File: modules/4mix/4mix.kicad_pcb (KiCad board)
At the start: 4 copper layers, 91.4 x 68.6 mm, 6 parts

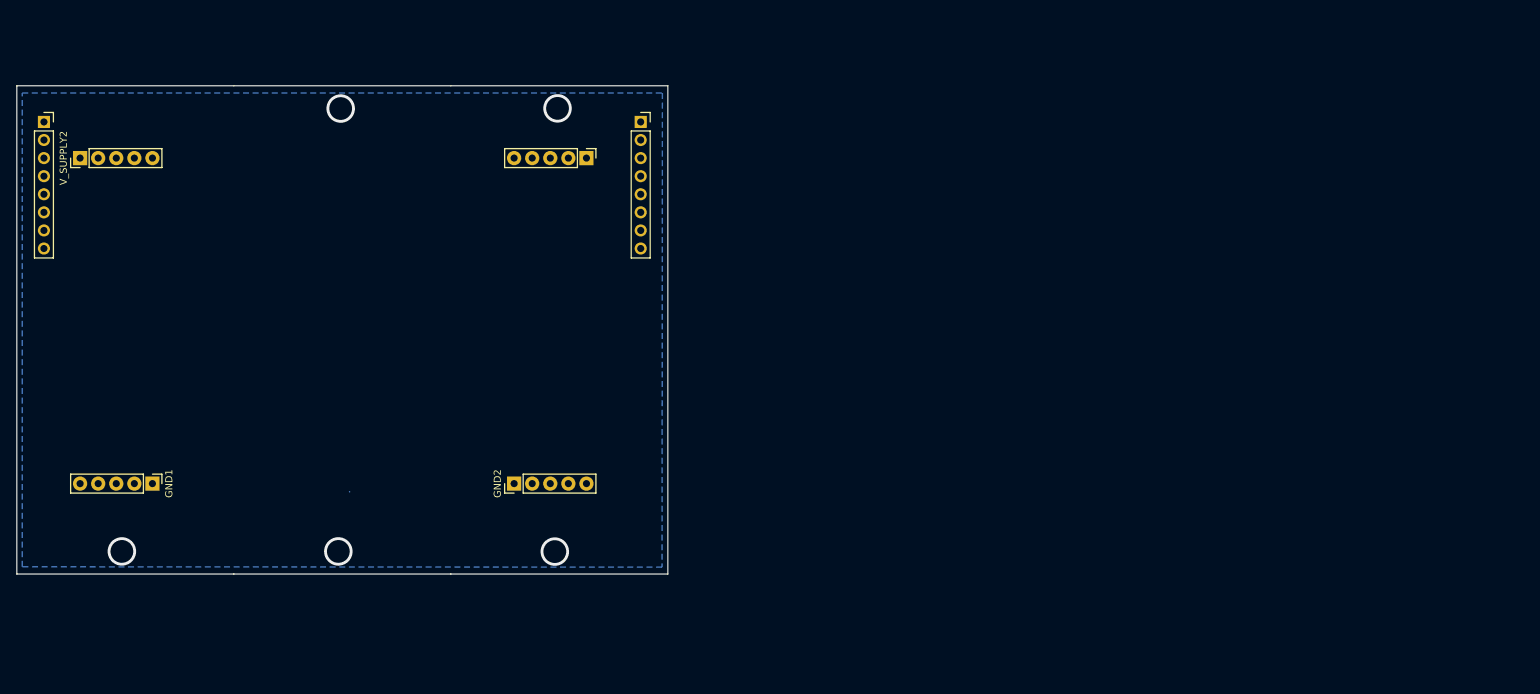
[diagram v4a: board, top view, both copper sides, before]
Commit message: Implement channel 1 routing
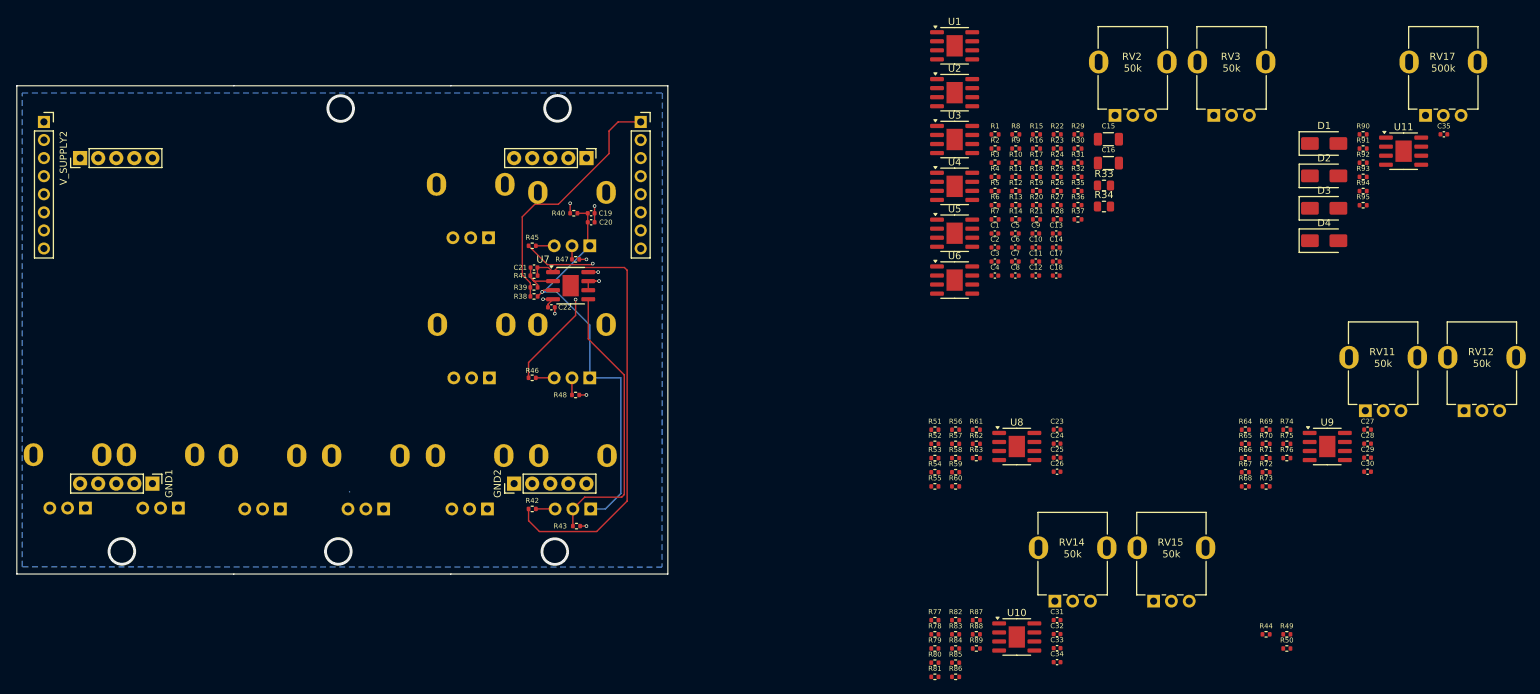
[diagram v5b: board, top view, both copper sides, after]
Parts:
- added C1: 100pf, Capacitor_SMD:C_0402_1005Metric, F.Cu at (184.4, 61.4)
- added C10: 47pf, Capacitor_SMD:C_0402_1005Metric, F.Cu at (190.1, 63.4)
- added C11: 0.1uf, Capacitor_SMD:C_0402_1005Metric, F.Cu at (190.1, 65.3)
- added C12: 0.1uf, Capacitor_SMD:C_0402_1005Metric, F.Cu at (190.1, 67.3)
- added C13: 0.1uf, Capacitor_SMD:C_0402_1005Metric, F.Cu at (193.0, 61.4)
- added C14: 0.1uf, Capacitor_SMD:C_0402_1005Metric, F.Cu at (193.0, 63.4)
- added C15: 0.1uf, Capacitor_SMD:C_1206_3216Metric, F.Cu at (200.3, 48.1)
- added C16: 100uf, Capacitor_SMD:C_1206_3216Metric, F.Cu at (200.3, 51.5)
- added C17: 0.1uf, Capacitor_SMD:C_0402_1005Metric, F.Cu at (193.0, 65.3)
- added C18: 0.1uf, Capacitor_SMD:C_0402_1005Metric, F.Cu at (193.0, 67.3)
- added C19: 10uf, Capacitor_SMD:C_0402_1005Metric, F.Cu at (127.7, 58.5)
- added C2: 100pf, Capacitor_SMD:C_0402_1005Metric, F.Cu at (184.4, 63.4)
- added C20: 0.1uf, Capacitor_SMD:C_0402_1005Metric, F.Cu at (127.7, 59.8)
- added C21: 47pf, Capacitor_SMD:C_0402_1005Metric, F.Cu at (119.6, 66.2)
- added C22: 0.1uf, Capacitor_SMD:C_0402_1005Metric, F.Cu at (122.1, 71.8)
- added C23: 10uf, Capacitor_SMD:C_0402_1005Metric, F.Cu at (193.1, 88.9)
- added C24: 0.1uf, Capacitor_SMD:C_0402_1005Metric, F.Cu at (193.1, 90.9)
- added C25: 47pf, Capacitor_SMD:C_0402_1005Metric, F.Cu at (193.1, 92.9)
- added C26: 0.1uf, Capacitor_SMD:C_0402_1005Metric, F.Cu at (193.1, 94.8)
- added C27: 10uf, Capacitor_SMD:C_0402_1005Metric, F.Cu at (236.7, 88.9)
- added C28: 0.1uf, Capacitor_SMD:C_0402_1005Metric, F.Cu at (236.7, 90.9)
- added C29: 47pf, Capacitor_SMD:C_0402_1005Metric, F.Cu at (236.7, 92.9)
- added C3: 47pf, Capacitor_SMD:C_0402_1005Metric, F.Cu at (184.4, 65.3)
- added C30: 0.1uf, Capacitor_SMD:C_0402_1005Metric, F.Cu at (236.7, 94.8)
- added C31: 10uf, Capacitor_SMD:C_0402_1005Metric, F.Cu at (193.1, 115.7)
- added C32: 0.1uf, Capacitor_SMD:C_0402_1005Metric, F.Cu at (193.1, 117.7)
- added C33: 47pf, Capacitor_SMD:C_0402_1005Metric, F.Cu at (193.1, 119.6)
- added C34: 0.1uf, Capacitor_SMD:C_0402_1005Metric, F.Cu at (193.1, 121.6)
- added C35: 0.1uf, Capacitor_SMD:C_0402_1005Metric, F.Cu at (247.4, 47.5)
- added C4: 47pf, Capacitor_SMD:C_0402_1005Metric, F.Cu at (184.4, 67.3)
- added C5: 47pf, Capacitor_SMD:C_0402_1005Metric, F.Cu at (187.2, 61.4)
- added C6: 47pf, Capacitor_SMD:C_0402_1005Metric, F.Cu at (187.2, 63.4)
- added C7: 47pf, Capacitor_SMD:C_0402_1005Metric, F.Cu at (187.2, 65.3)
- added C8: 47pf, Capacitor_SMD:C_0402_1005Metric, F.Cu at (187.2, 67.3)
- added C9: 47pf, Capacitor_SMD:C_0402_1005Metric, F.Cu at (190.1, 61.4)
- added D1: SS14, Diode_SMD:D_SMA, F.Cu at (230.6, 48.8)
- added D2: SS14, Diode_SMD:D_SMA, F.Cu at (230.6, 53.3)
- added D3: SS14, Diode_SMD:D_SMA, F.Cu at (230.6, 57.9)
- added D4: SS210, Diode_SMD:D_SMA, F.Cu at (230.6, 62.4)
- added R1: 1M, Resistor_SMD:R_0402_1005Metric, F.Cu at (184.4, 47.5)
- added R10: 100, Resistor_SMD:R_0402_1005Metric, F.Cu at (187.3, 51.5)
- added R11: 56k, Resistor_SMD:R_0402_1005Metric, F.Cu at (187.3, 53.4)
- added R12: 100, Resistor_SMD:R_0402_1005Metric, F.Cu at (187.3, 55.4)
- added R13: 100, Resistor_SMD:R_0402_1005Metric, F.Cu at (187.3, 57.4)
- added R14: 56k, Resistor_SMD:R_0402_1005Metric, F.Cu at (187.3, 59.4)
- added R15: 56k, Resistor_SMD:R_0402_1005Metric, F.Cu at (190.2, 47.5)
- added R16: 56k, Resistor_SMD:R_0402_1005Metric, F.Cu at (190.2, 49.5)
- added R17: 56k, Resistor_SMD:R_0402_1005Metric, F.Cu at (190.2, 51.5)
- added R18: 56k, Resistor_SMD:R_0402_1005Metric, F.Cu at (190.2, 53.4)
- added R19: 1M, Resistor_SMD:R_0402_1005Metric, F.Cu at (190.2, 55.4)
- added R2: 56k, Resistor_SMD:R_0402_1005Metric, F.Cu at (184.4, 49.5)
- added R20: 1M, Resistor_SMD:R_0402_1005Metric, F.Cu at (190.2, 57.4)
- added R21: 56k, Resistor_SMD:R_0402_1005Metric, F.Cu at (190.2, 59.4)
- added R22: 56k, Resistor_SMD:R_0402_1005Metric, F.Cu at (193.1, 47.5)
- added R23: 56k, Resistor_SMD:R_0402_1005Metric, F.Cu at (193.1, 49.5)
- added R24: 56k, Resistor_SMD:R_0402_1005Metric, F.Cu at (193.1, 51.5)
- added R25: 56k, Resistor_SMD:R_0402_1005Metric, F.Cu at (193.1, 53.4)
- added R26: 1k, Resistor_SMD:R_0402_1005Metric, F.Cu at (193.1, 55.4)
- added R27: 100, Resistor_SMD:R_0402_1005Metric, F.Cu at (193.1, 57.4)
- added R28: 100, Resistor_SMD:R_0402_1005Metric, F.Cu at (193.1, 59.4)
- added R29: 56k, Resistor_SMD:R_0402_1005Metric, F.Cu at (196.0, 47.5)
- added R3: 10k, Resistor_SMD:R_0402_1005Metric, F.Cu at (184.4, 51.5)
- added R30: 56k, Resistor_SMD:R_0402_1005Metric, F.Cu at (196.0, 49.5)
- added R31: 56k, Resistor_SMD:R_0402_1005Metric, F.Cu at (196.0, 51.5)
- added R32: 56k, Resistor_SMD:R_0402_1005Metric, F.Cu at (196.0, 53.4)
- added R33: 330, Resistor_SMD:R_0805_2012Metric, F.Cu at (199.7, 54.6)
- added R34: 330, Resistor_SMD:R_0805_2012Metric, F.Cu at (199.7, 57.6)
- added R35: 10k, Resistor_SMD:R_0402_1005Metric, F.Cu at (196.0, 55.4)
- added R36: 10k, Resistor_SMD:R_0402_1005Metric, F.Cu at (196.0, 57.4)
- added R37: 10, Resistor_SMD:R_0402_1005Metric, F.Cu at (196.0, 59.4)
- added R38: 1M, Resistor_SMD:R_0402_1005Metric, F.Cu at (119.6, 70.2)
- added R39: 56k, Resistor_SMD:R_0402_1005Metric, F.Cu at (119.6, 69.0)
- added R4: 10k, Resistor_SMD:R_0402_1005Metric, F.Cu at (184.4, 53.4)
- added R40: 100, Resistor_SMD:R_0402_1005Metric, F.Cu at (125.2, 58.5)
- added R41: 56k, Resistor_SMD:R_0402_1005Metric, F.Cu at (119.6, 67.3)
- added R42: 100, Resistor_SMD:R_0402_1005Metric, F.Cu at (119.4, 100.1)
- added R43: 100, Resistor_SMD:R_0402_1005Metric, F.Cu at (125.6, 102.5)
- added R44: 56k, Resistor_SMD:R_0402_1005Metric, F.Cu at (222.5, 117.7)
- added R45: 100, Resistor_SMD:R_0402_1005Metric, F.Cu at (119.4, 63.1)
- added R46: 100, Resistor_SMD:R_0402_1005Metric, F.Cu at (119.4, 81.7)
- added R47: 100, Resistor_SMD:R_0402_1005Metric, F.Cu at (125.5, 65.0)
- added R48: 100, Resistor_SMD:R_0402_1005Metric, F.Cu at (125.5, 84.1)
- added R49: 56k, Resistor_SMD:R_0402_1005Metric, F.Cu at (225.4, 117.7)
- added R5: 56k, Resistor_SMD:R_0402_1005Metric, F.Cu at (184.4, 55.4)
- added R50: 56k, Resistor_SMD:R_0402_1005Metric, F.Cu at (225.4, 119.7)
- added R51: 1M, Resistor_SMD:R_0402_1005Metric, F.Cu at (175.9, 89.0)
- added R52: 56k, Resistor_SMD:R_0402_1005Metric, F.Cu at (175.9, 90.9)
- added R53: 100, Resistor_SMD:R_0402_1005Metric, F.Cu at (175.9, 92.9)
- added R54: 56k, Resistor_SMD:R_0402_1005Metric, F.Cu at (175.9, 94.9)
- added R55: 100, Resistor_SMD:R_0402_1005Metric, F.Cu at (175.9, 96.9)
- added R56: 100, Resistor_SMD:R_0402_1005Metric, F.Cu at (178.8, 89.0)
- added R57: 56k, Resistor_SMD:R_0402_1005Metric, F.Cu at (178.8, 90.9)
- added R58: 100, Resistor_SMD:R_0402_1005Metric, F.Cu at (178.8, 92.9)
- added R59: 100, Resistor_SMD:R_0402_1005Metric, F.Cu at (178.8, 94.9)
- added R6: 1M, Resistor_SMD:R_0402_1005Metric, F.Cu at (184.4, 57.4)
- added R60: 100, Resistor_SMD:R_0402_1005Metric, F.Cu at (178.8, 96.9)
- added R61: 100, Resistor_SMD:R_0402_1005Metric, F.Cu at (181.8, 89.0)
- added R62: 56k, Resistor_SMD:R_0402_1005Metric, F.Cu at (181.8, 90.9)
- added R63: 56k, Resistor_SMD:R_0402_1005Metric, F.Cu at (181.8, 92.9)
- added R64: 1M, Resistor_SMD:R_0402_1005Metric, F.Cu at (219.6, 89.0)
- added R65: 56k, Resistor_SMD:R_0402_1005Metric, F.Cu at (219.6, 90.9)
- added R66: 100, Resistor_SMD:R_0402_1005Metric, F.Cu at (219.6, 92.9)
- added R67: 56k, Resistor_SMD:R_0402_1005Metric, F.Cu at (219.6, 94.9)
- added R68: 100, Resistor_SMD:R_0402_1005Metric, F.Cu at (219.6, 96.9)
- added R69: 100, Resistor_SMD:R_0402_1005Metric, F.Cu at (222.5, 89.0)
- added R7: 1M, Resistor_SMD:R_0402_1005Metric, F.Cu at (184.4, 59.4)
- added R70: 56k, Resistor_SMD:R_0402_1005Metric, F.Cu at (222.5, 90.9)
- added R71: 100, Resistor_SMD:R_0402_1005Metric, F.Cu at (222.5, 92.9)
- added R72: 100, Resistor_SMD:R_0402_1005Metric, F.Cu at (222.5, 94.9)
- added R73: 100, Resistor_SMD:R_0402_1005Metric, F.Cu at (222.5, 96.9)
- added R74: 100, Resistor_SMD:R_0402_1005Metric, F.Cu at (225.4, 89.0)
- added R75: 56k, Resistor_SMD:R_0402_1005Metric, F.Cu at (225.4, 90.9)
- added R76: 56k, Resistor_SMD:R_0402_1005Metric, F.Cu at (225.4, 92.9)
- added R77: 1M, Resistor_SMD:R_0402_1005Metric, F.Cu at (175.9, 115.7)
- added R78: 56k, Resistor_SMD:R_0402_1005Metric, F.Cu at (175.9, 117.7)
- added R79: 100, Resistor_SMD:R_0402_1005Metric, F.Cu at (175.9, 119.7)
- added R8: 56k, Resistor_SMD:R_0402_1005Metric, F.Cu at (187.3, 47.5)
- added R80: 56k, Resistor_SMD:R_0402_1005Metric, F.Cu at (175.9, 121.7)
- added R81: 100, Resistor_SMD:R_0402_1005Metric, F.Cu at (175.9, 123.7)
- added R82: 100, Resistor_SMD:R_0402_1005Metric, F.Cu at (178.8, 115.7)
- added R83: 56k, Resistor_SMD:R_0402_1005Metric, F.Cu at (178.8, 117.7)
- added R84: 100, Resistor_SMD:R_0402_1005Metric, F.Cu at (178.8, 119.7)
- added R85: 100, Resistor_SMD:R_0402_1005Metric, F.Cu at (178.8, 121.7)
- added R86: 100, Resistor_SMD:R_0402_1005Metric, F.Cu at (178.8, 123.7)
- added R87: 100, Resistor_SMD:R_0402_1005Metric, F.Cu at (181.8, 115.7)
- added R88: 56k, Resistor_SMD:R_0402_1005Metric, F.Cu at (181.8, 117.7)
- added R89: 56k, Resistor_SMD:R_0402_1005Metric, F.Cu at (181.8, 119.7)
- added R9: 100, Resistor_SMD:R_0402_1005Metric, F.Cu at (187.3, 49.5)
- added R90: 100k, Resistor_SMD:R_0402_1005Metric, F.Cu at (236.1, 47.5)
- added R91: 100k, Resistor_SMD:R_0402_1005Metric, F.Cu at (236.1, 49.5)
- added R92: 1k, Resistor_SMD:R_0402_1005Metric, F.Cu at (236.1, 51.5)
- added R93: 51k, Resistor_SMD:R_0402_1005Metric, F.Cu at (236.1, 53.4)
- added R94: 1k, Resistor_SMD:R_0402_1005Metric, F.Cu at (236.1, 55.4)
- added R95: 1k, Resistor_SMD:R_0402_1005Metric, F.Cu at (236.1, 57.4)
- added RV1: 50k, BreadModular_Pots:Potentiometer_RV09, B.Cu at (67.1, 93.0)
- added RV10: 50k, BreadModular_Pots:Potentiometer_RV09, B.Cu at (95.9, 93.1)
- added RV11: 50k, BreadModular_Pots:Potentiometer_RV09, F.Cu at (239.0, 79.3)
- added RV12: 50k, BreadModular_Pots:Potentiometer_RV09, F.Cu at (252.9, 79.3)
- added RV13: 50k, BreadModular_Pots:Potentiometer_RV09, B.Cu at (81.4, 93.1)
- added RV14: 50k, BreadModular_Pots:Potentiometer_RV09, F.Cu at (195.4, 106.0)
- added RV15: 50k, BreadModular_Pots:Potentiometer_RV09, F.Cu at (209.3, 106.0)
- added RV16: 50k, BreadModular_Pots:Potentiometer_RV09, B.Cu at (54.0, 93.0)
- added RV17: 500k, BreadModular_Pots:Potentiometer_RV09, F.Cu at (247.5, 37.8)
- added RV2: 50k, BreadModular_Pots:Potentiometer_RV09, F.Cu at (203.9, 37.8)
- added RV3: 50k, BreadModular_Pots:Potentiometer_RV09, F.Cu at (217.7, 37.8)
- added RV4: 50k, BreadModular_Pots:Potentiometer_RV09, B.Cu at (125.0, 93.1)
- added RV5: 50k, BreadModular_Pots:Potentiometer_RV09, B.Cu at (124.8, 56.1)
- added RV6: 50k, BreadModular_Pots:Potentiometer_RV09, B.Cu at (124.8, 74.7)
- added RV7: 50k, BreadModular_Pots:Potentiometer_RV09, B.Cu at (110.5, 93.1)
- added RV8: 50k, BreadModular_Pots:Potentiometer_RV09, B.Cu at (110.6, 55.0)
- added RV9: 50k, BreadModular_Pots:Potentiometer_RV09, B.Cu at (110.7, 74.7)
- added U1: MCP6002-xSN, Package_SO:SOIC-8-1EP_3.9x4.9mm_P1.27mm_EP2.29x3mm, F.Cu at (178.7, 35.0)
- added U10: MCP6002-xSN, Package_SO:SOIC-8-1EP_3.9x4.9mm_P1.27mm_EP2.29x3mm, F.Cu at (187.4, 118.1)
- added U11: MCP6002-xSN, Package_SO:SOIC-8-1EP_3.9x4.9mm_P1.27mm_EP2.29x3mm, F.Cu at (241.8, 49.8)
- added U2: MCP6002-xSN, Package_SO:SOIC-8-1EP_3.9x4.9mm_P1.27mm_EP2.29x3mm, F.Cu at (178.7, 41.6)
- added U3: MCP6002-xSN, Package_SO:SOIC-8-1EP_3.9x4.9mm_P1.27mm_EP2.29x3mm, F.Cu at (178.7, 48.2)
- added U4: MCP6002-xSN, Package_SO:SOIC-8-1EP_3.9x4.9mm_P1.27mm_EP2.29x3mm, F.Cu at (178.7, 54.8)
- added U5: MCP6002-xSN, Package_SO:SOIC-8-1EP_3.9x4.9mm_P1.27mm_EP2.29x3mm, F.Cu at (178.7, 61.4)
- added U6: MCP6002-xSN, Package_SO:SOIC-8-1EP_3.9x4.9mm_P1.27mm_EP2.29x3mm, F.Cu at (178.7, 67.9)
- added U7: MCP6002-xSN, Package_SO:SOIC-8-1EP_3.9x4.9mm_P1.27mm_EP2.29x3mm, F.Cu at (124.8, 68.7)
- added U8: MCP6002-xSN, Package_SO:SOIC-8-1EP_3.9x4.9mm_P1.27mm_EP2.29x3mm, F.Cu at (187.4, 91.3)
- added U9: MCP6002-xSN, Package_SO:SOIC-8-1EP_3.9x4.9mm_P1.27mm_EP2.29x3mm, F.Cu at (231.1, 91.3)
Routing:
- net Net-(C21-Pad2): track 0.00 -> 64.8 mm
- net V_MID_1: track 0.00 -> 59.8 mm, vias 0 -> 1
- net Net-(U7B-+): track 0.00 -> 40.0 mm
- net IN_1: track 0.00 -> 35.7 mm
- net Net-(U7B--): track 0.00 -> 33.9 mm, vias 0 -> 3
- net Net-(U7A--): track 0.00 -> 6.08 mm
- net GND: track 0.00 -> 5.11 mm, vias 0 -> 2
- net Net-(R42-Pad2): track 0.00 -> 2.71 mm
- net Net-(R46-Pad2): track 0.00 -> 2.60 mm
- net Net-(R45-Pad2): track 0.00 -> 2.58 mm
- net Net-(R48-Pad1): track 0.00 -> 2.40 mm
- net V_SUPPLY: track 0.00 -> 2.29 mm, vias 0 -> 2
- net Net-(R47-Pad1): track 0.00 -> 1.91 mm
- net V_MID: track 0.00 -> 1.40 mm, vias 1 -> 2
- net Net-(R48-Pad2): track 0.00 -> 1.02 mm, vias 0 -> 1
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
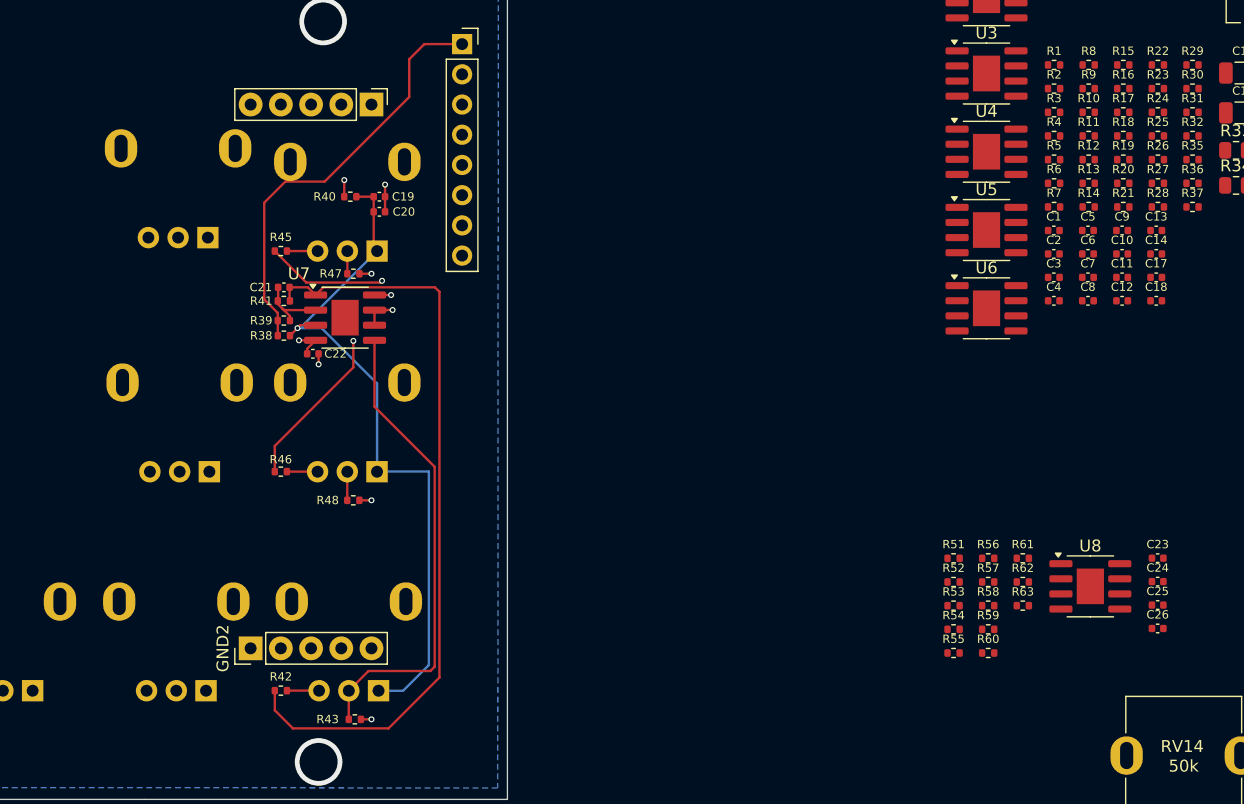
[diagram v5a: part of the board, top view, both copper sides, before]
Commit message: Routed channel 2
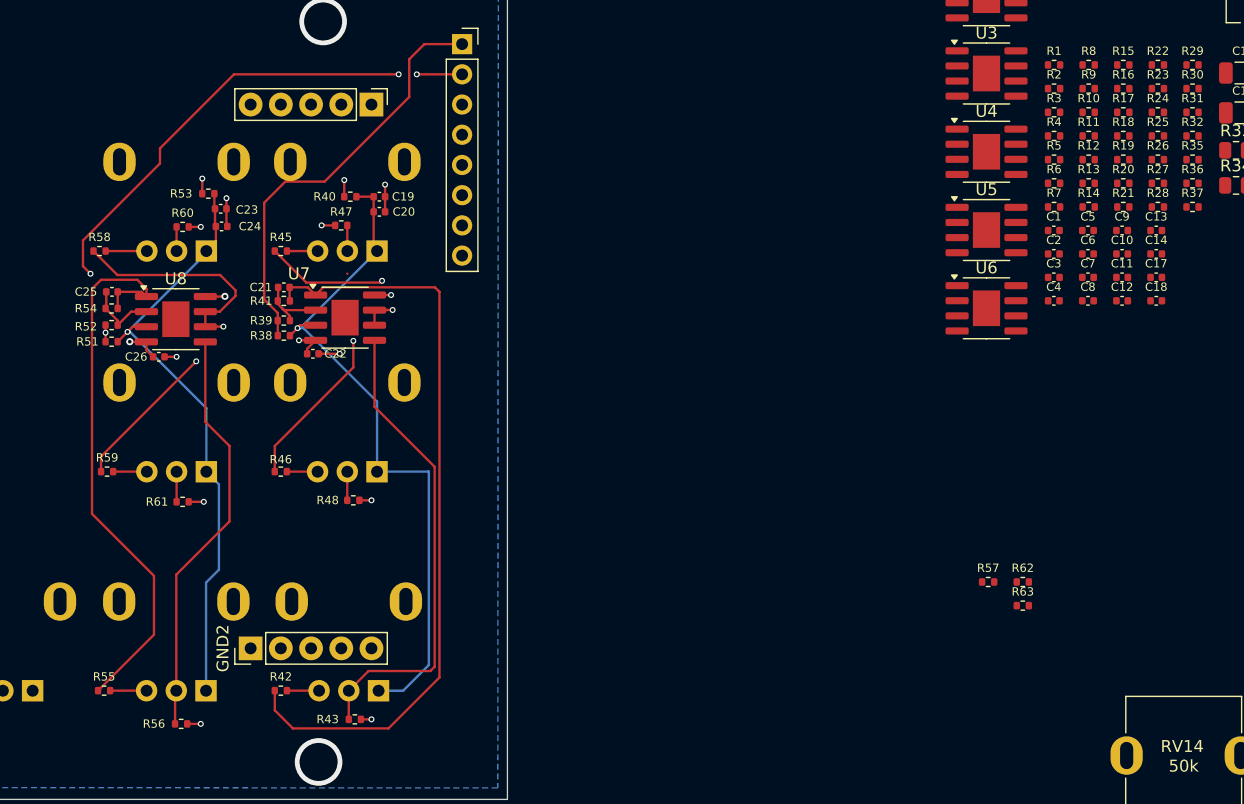
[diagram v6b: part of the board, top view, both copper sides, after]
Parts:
- moved C25 91.8 mm to (105.2, 66.5)
- moved C26 87.0 mm to (109.1, 72.0), turned to 180 degrees
- moved C24 84.2 mm to (114.4, 61.0)
- moved C23 84.1 mm to (114.3, 59.6)
- moved R58 80.4 mm to (104.1, 63.1)
- moved U8 80.1 mm to (110.6, 68.8)
- moved R60 76.6 mm to (111.1, 61.1)
- moved R54 75.8 mm to (105.2, 67.9)
- moved R59 75.3 mm to (104.8, 81.7)
- moved R52 74.0 mm to (105.2, 69.3)
- moved R51 73.1 mm to (105.2, 70.7), turned to 180 degrees
- moved R53 71.6 mm to (113.3, 58.3), turned to 180 degrees
- moved R55 71.5 mm to (104.5, 100.1)
- moved R61 70.8 mm to (111.1, 84.2)
- moved R56 69.3 mm to (111.0, 102.9)
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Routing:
- net V_MID_2: track 0.00 -> 51.6 mm, vias 0 -> 1
- net IN_2: track 0.00 -> 48.3 mm, vias 0 -> 4
- net Net-(C25-Pad2): track 0.00 -> 47.7 mm
- net Net-(U8B--): track 0.00 -> 36.1 mm, vias 0 -> 2
- net Net-(U8B-+): track 0.00 -> 34.9 mm
- net Net-(U8A--): track 0.00 -> 6.13 mm
- net GND: track 5.11 -> 10.4 mm, vias 2 -> 4
- net V_SUPPLY: track 2.29 -> 5.85 mm, vias 2 -> 4
- net Net-(R58-Pad2): track 0.00 -> 3.47 mm
- net Net-(R55-Pad2): track 0.00 -> 3.06 mm
- net Net-(R59-Pad2): track 0.00 -> 2.84 mm
- net Net-(R61-Pad1): track 0.00 -> 2.53 mm
- net Net-(R60-Pad1): track 0.00 -> 2.03 mm
- net V_MID: track 1.40 -> 2.67 mm, vias 2 -> 3
- net Net-(R61-Pad2): track 0.00 -> 1.27 mm, vias 0 -> 1
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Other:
- board text added: "4MIX 0.5.0"
- board text removed: "4MIX 0.4.0"

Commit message: add channel 3 routing
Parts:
- RV11, RV12: moved to B.Cu
- moved RV12 157.2 mm to (95.8, 74.7), turned to 180 degrees
- moved C29 148.4 mm to (90.6, 66.9)
- moved RV11 145.2 mm to (95.7, 56.1), turned to 180 degrees
- moved C30 144.3 mm to (94.2, 72.2), turned to 180 degrees
- moved C28 140.2 mm to (99.8, 60.9)
- moved C27 140.1 mm to (99.8, 59.4)
- moved U9 137.2 mm to (95.7, 68.9)
- moved R71 136.6 mm to (89.2, 63.1)
- moved R72 133.1 mm to (90.0, 81.7)
- moved R67 131.7 mm to (90.6, 68.3)
- moved R73 131.2 mm to (96.3, 60.9)
- moved R65 130.8 mm to (90.5, 69.6)
- moved R64 130.3 mm to (90.5, 70.9), turned to 180 degrees
- moved R68 130.1 mm to (89.5, 100.1)
- moved R74 129.1 mm to (96.3, 84.1)
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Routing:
- net IN_3: track 0.00 -> 64.3 mm, vias 0 -> 4
- net V_MID_3: track 0.00 -> 52.1 mm, vias 0 -> 1
- net Net-(C29-Pad2): track 0.00 -> 44.1 mm
- net Net-(U9B--): track 0.00 -> 37.9 mm, vias 0 -> 2
- net Net-(U9B-+): track 0.00 -> 35.7 mm
- net Net-(U9A--): track 0.00 -> 7.18 mm
- net GND: track 10.4 -> 14.4 mm, vias 4 -> 6
- net Net-(R71-Pad2): track 0.00 -> 3.64 mm
- net Net-(R68-Pad2): track 0.00 -> 3.47 mm
- net Net-(R72-Pad2): track 0.00 -> 2.83 mm
- net V_SUPPLY: track 5.85 -> 8.49 mm, vias 4 -> 6
- net Net-(R74-Pad1): track 0.00 -> 2.50 mm
- net Net-(R73-Pad1): track 0.00 -> 2.27 mm
- net Net-(R74-Pad2): track 0.00 -> 1.29 mm, vias 0 -> 1
- net Net-(R73-Pad2): track 0.00 -> 1.09 mm, vias 0 -> 1
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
